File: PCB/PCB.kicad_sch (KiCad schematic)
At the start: 1 part, among them J19 Free_GPIO

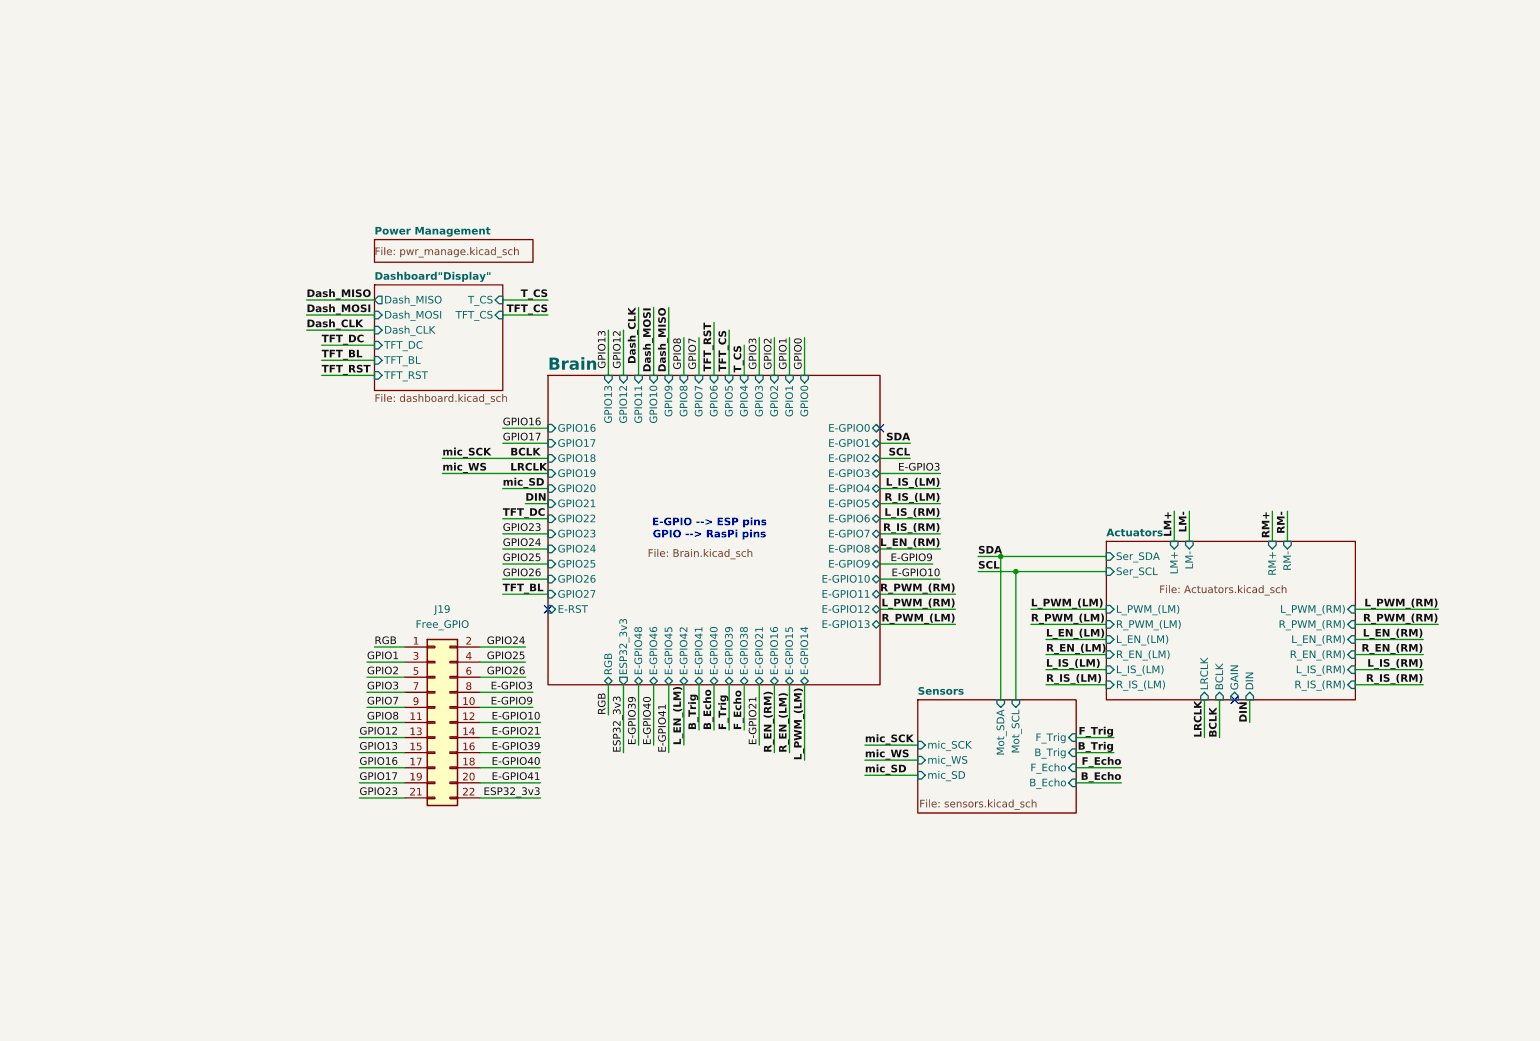
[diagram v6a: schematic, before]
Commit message: [PCB] Splited the PCB into two boards
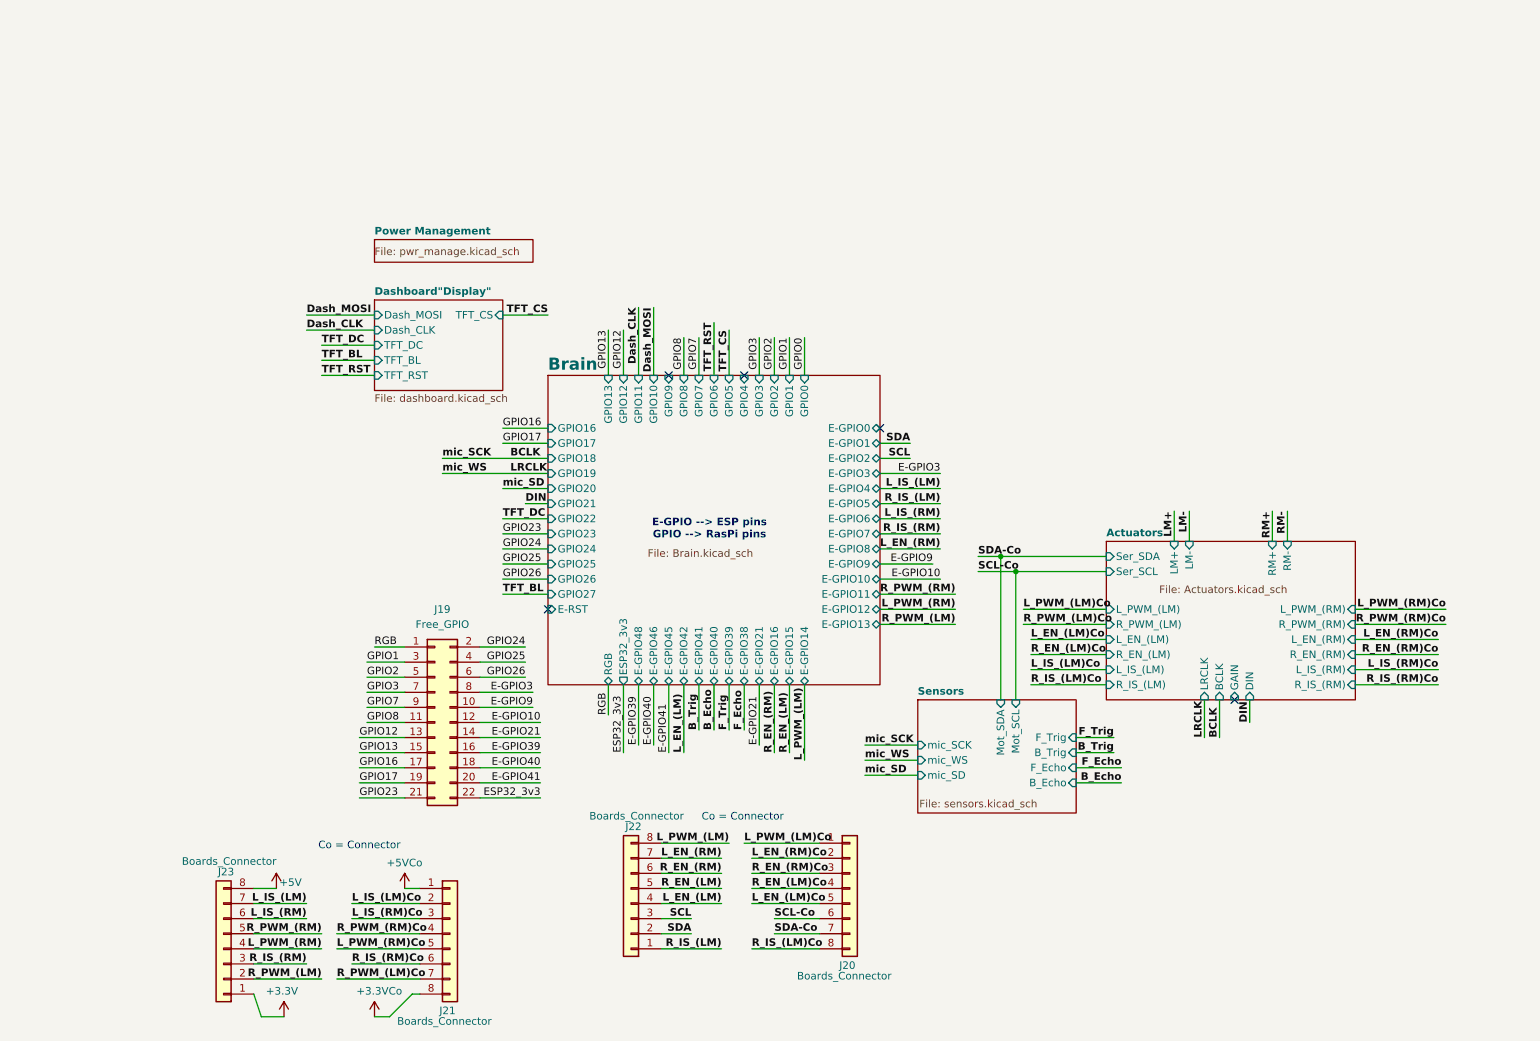
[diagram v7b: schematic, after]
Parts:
- added J20, J21, J22, J23: Boards_Connector, Connector_JST:JST_ZH_B8B-ZR-SM4-TF_1x08-1MP_P1.50mm_Vertical, symbol Connector_Generic:Conn_01x08
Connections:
- net L_EN_(LM): now also J22.4 (Pin_4)
- net L_EN_(RM): now also J22.7 (Pin_7)
- net L_IS_(LM): now also J23.7 (Pin_7)
- net L_IS_(RM): now also J23.6 (Pin_6)
- net L_PWM_(LM): now also J22.8 (Pin_8)
- net L_PWM_(RM): now also J23.4 (Pin_4)
- net R_EN_(LM): now also J22.5 (Pin_5)
- net R_EN_(RM): now also J22.6 (Pin_6)
- net R_IS_(LM): now also J22.1 (Pin_1)
- net R_IS_(RM): now also J23.3 (Pin_3)
- net R_PWM_(LM): now also J23.2 (Pin_2)
- net R_PWM_(RM): now also J23.5 (Pin_5)
- net SCL: now also J22.3 (Pin_3)
- net SDA: now also J22.2 (Pin_2)
- new net +3.3V: J23.1 (Pin_1)
- new net +3.3VCo: J21.8 (Pin_8)
- new net +5V: J23.8 (Pin_8)
- new net +5VCo: J21.1 (Pin_1)
- new net L_EN_(LM)Co: J20.5 (Pin_5)
- new net L_EN_(RM)Co: J20.2 (Pin_2)
- new net L_IS_(LM)Co: J21.2 (Pin_2)
- new net L_IS_(RM)Co: J21.3 (Pin_3)
- new net L_PWM_(LM)Co: J20.1 (Pin_1)
- new net L_PWM_(RM)Co: J21.5 (Pin_5)
- new net R_EN_(LM)Co: J20.4 (Pin_4)
- new net R_EN_(RM)Co: J20.3 (Pin_3)
- new net R_IS_(LM)Co: J20.8 (Pin_8)
- new net R_IS_(RM)Co: J21.6 (Pin_6)
- new net R_PWM_(LM)Co: J21.7 (Pin_7)
- new net R_PWM_(RM)Co: J21.4 (Pin_4)
- new net SCL-Co: J20.6 (Pin_6)
- new net SDA-Co: J20.7 (Pin_7)
- no-connect marks 3 -> 5
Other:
- sheet Dashboard"Display" ports: added none; removed Dash_MISO, T_CS
- note added: "Co = Connector"
